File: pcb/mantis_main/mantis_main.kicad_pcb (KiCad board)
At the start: 2 copper layers, 239.5 x 120.4 mm, 114 parts, among them J3 nice!nano extra, J4 Pin Header, J5 JST-PH, J6 Conn_01x02_Socket, M1 SW_Mouse, M2 SW_Mouse, SW1 SW_SPDT, U1 74LVC1G17

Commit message: pcb: Routed mantis_main PCB
This PCB should be mostly done.

TODO:
1. check design rules and fix any issues.
2. Add a notch for the cable to the back of the PCB.

Signed-off-by: Felix Kuehling <felix.kuehling@gmail.com>
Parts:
- added J7: Conn_01x02_Socket, Connector_JST:JST_PH_S2B-PH-K_1x02_P2.00mm_Horizontal, B.Cu at (252.0, 70.2)
- moved J6 3.39 mm to (252.0, 70.2)
- moved R2 3.35 mm to (252.5, 72.9), turned to 90 degrees
- moved R3 3.35 mm to (254.0, 72.9), turned to 90 degrees
- moved FB1 0.76 mm to (248.9, 73.2)
- moved JP10 0.25 mm to (250.4, 84.3)
- moved JP2 0.25 mm to (250.4, 77.7)
- moved JP9 0.25 mm to (249.7, 80.2)
- moved R1 0.25 mm to (249.7, 82.3)
- moved U1 0.25 mm to (253.0, 80.8)
- turned LED10 to 120 degrees
- turned LED11 to 120 degrees
- turned LED12 to 0 degrees
- turned LED17 to 60 degrees
- turned LED21 to 180 degrees
- turned LED22 to -120 degrees
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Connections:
- net Net-(J1-5V) renamed VIK_5V
- net Net-(J6-Pin_2) renamed BAT
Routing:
- net LED_VCC: track 53.4 -> 962.8 mm, vias 3 -> 17
- net C2: track 11.7 -> 293.6 mm, vias 1 -> 6
- net L3: track 0.00 -> 262.0 mm
- net C3: track 13.7 -> 245.8 mm, vias 1 -> 7
- net R3: track 0.00 -> 202.5 mm
- net C7: track 20.9 -> 185.7 mm, vias 1 -> 4
- net L2: track 35.4 -> 184.7 mm, vias 1 -> 3
- net C4: track 15.1 -> 159.8 mm, vias 1 -> 5
- net C1: track 186.7 -> 330.1 mm, vias 1 -> 10
- net Net-(LED13-DOUT): track 0.00 -> 141.9 mm, vias 0 -> 2
- net R2: track 28.8 -> 144.2 mm
- net C6: track 23.7 -> 133.0 mm, vias 1 -> 2
- net L1: track 31.7 -> 140.3 mm, vias 1 -> 3
- net C5: track 84.7 -> 177.1 mm, vias 1 -> 3
- net Net-(LED12-DOUT): track 0.00 -> 55.3 mm
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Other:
- board text added: "+ - +"
- board text added: "Battery"

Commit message: pcb/mantis_main: Fixes and tweaks
Corrected the matrix to match Ergogen: 3 bottom row keys use C2, C3, C4.
C1 keeps one extra spot for the raised PCB.

Added jumper to bypass the ferrite bead.

Repositioned ferrite bead to give it more solid GND connection.

Minor position tweaks for battery switch, and display connector.

Many routing improvements, more ground vias.

Added Mantis graphic, VIK logo and signature.

Signed-off-by: Felix Kuehling <felix.kuehling@gmail.com>
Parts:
- added JP11: Bypass FB1, Jumper:SolderJumper-2_P1.3mm_Open_RoundedPad1.0x1.5mm, B.Cu at (251.7, 75.3)
- added REF**: vik-logo-medium, Vik:vik-logo-medium, F.Cu at (278.3, 87.9)
- moved FB1 14.4 mm to (259.6, 63.5), turned to 90 degrees
- moved SW1 0.16 mm to (254.0, 62.9)
- moved J5 0.06 mm to (258.0, 90.7)
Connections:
- S1 pad 2: C1 -> C2
- S14 pad 2: C1 -> C2
- S15 pad 2: C2 -> C3
- S16 pad 2: C3 -> C4
- S2 pad 2: C2 -> C3
- S3 pad 2: C3 -> C4
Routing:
- net R3: track 202.5 -> 267.9 mm, vias 0 -> 2
- net R1: track 75.9 -> 123.6 mm
- net C4: track 159.8 -> 196.6 mm, vias 5 -> 6
- net C1: track 330.1 -> 297.1 mm, vias 10 -> 8
- net LED_VCC: track 962.8 -> 989.9 mm
- net L2: track 184.7 -> 165.6 mm, vias 3 -> 5
- net GND: track 19.8 -> 13.2 mm, vias 16 -> 34
- net GNDPWR: track 22.6 -> 28.7 mm
- net L1: track 140.3 -> 144.5 mm
- net SPICS_or_GPIO1: track 17.1 -> 20.7 mm
- net C3: track 245.8 -> 242.8 mm
- net C2: track 293.6 -> 290.7 mm
- net R2: track 144.2 -> 146.6 mm
- net Net-(LED3-DIN): track 36.2 -> 33.8 mm, vias 0 -> 2
- net RAW: track 12.2 -> 14.0 mm
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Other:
- board text added: "Bypass FB1"
- board text added: "Mantis v1.0 Felix Kühling Jan 2026"

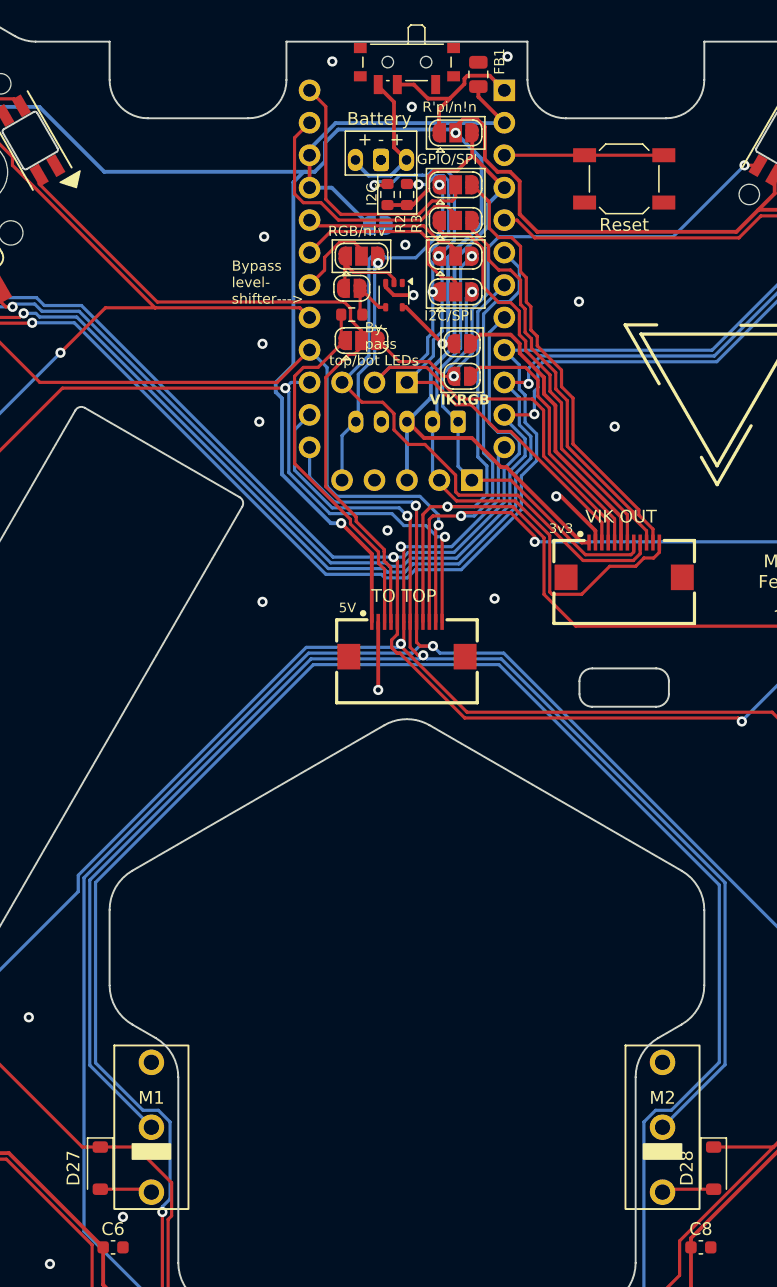
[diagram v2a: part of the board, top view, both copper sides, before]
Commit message: pcb: Reposition battery connector
Renumbered connectors to match updated ergogen, which now includes the
battery connector. Removed second battery connector again.

Updated PCB and routing to wire up the connector in the new location and
take advantage of the freed-up real-estate under the controller.

Signed-off-by: Felix Kuehling <felix.kuehling@gmail.com>
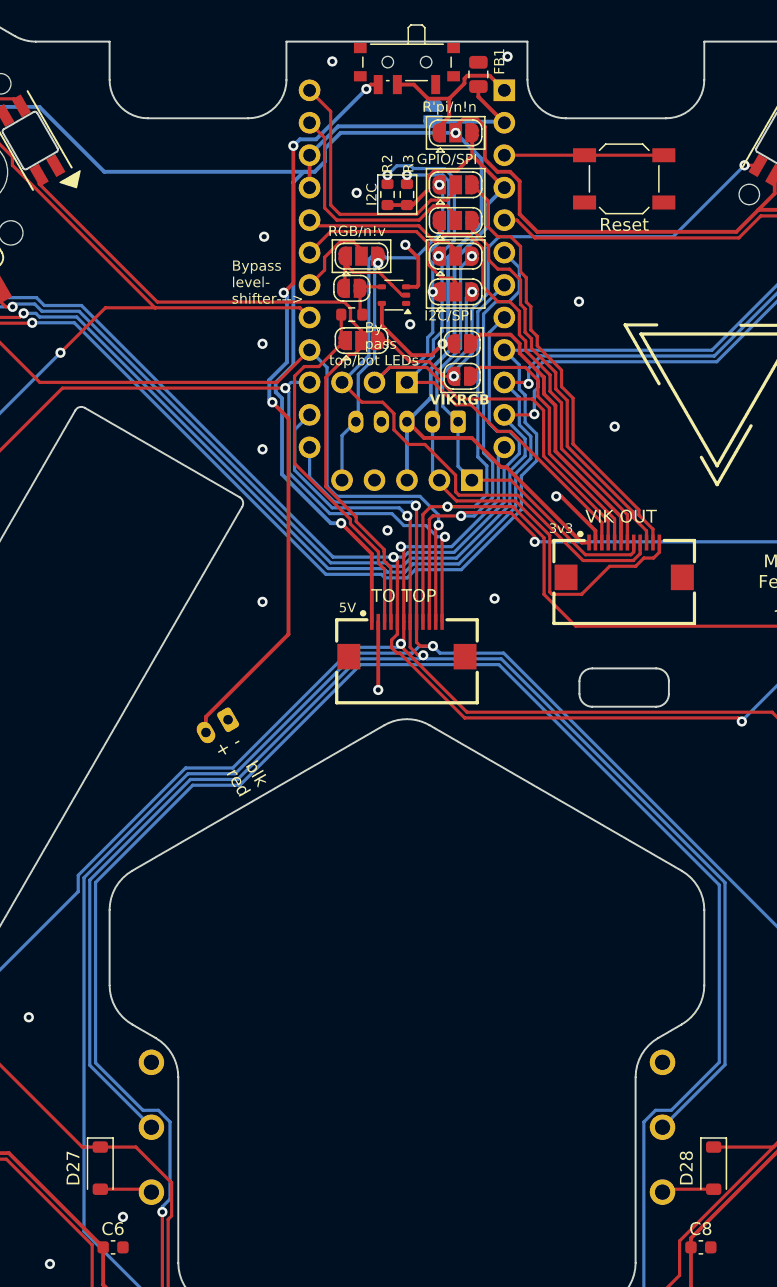
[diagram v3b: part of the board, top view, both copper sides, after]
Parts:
- removed J7: Conn_01x02_Socket, Connector_JST:JST_PH_S2B-PH-K_1x02_P2.00mm_Horizontal
- M1, M2: moved to B.Cu
- moved J4 45.4 mm to (240.0, 114.0), turned to -150 degrees
- moved JP11 9.77 mm to (256.0, 66.5), turned to 90 degrees
- turned M1 to 180 degrees
- turned M2 to 180 degrees
- turned U1 to 180 degrees
- renumbered J6 to J4, J4 to J5, J5 to J6
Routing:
- net BAT: track 12.1 -> 59.1 mm, vias 0 -> 4
- net GNDPWR: track 28.7 -> 22.6 mm
- net LED_VCC: track 989.9 -> 992.9 mm
- net GND: track 13.2 -> 15.0 mm
- net SPICS_or_GPIO1: track 20.7 -> 19.0 mm
- net SDA: track 47.2 -> 45.8 mm
- net LED: track 7.81 -> 8.96 mm
- net TOP_LED: track 4.75 -> 3.88 mm
- net RAW: track 14.0 -> 13.3 mm
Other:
- board text added: "+ -"
- board text added: "blk red"
- board text removed: "+ - +"
- board text removed: "Battery"
